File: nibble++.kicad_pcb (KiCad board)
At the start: 2 copper layers, 40 x 40 mm, 22 parts, among them SW1 SW_DPDT_x2, U1 NE555, U2 4017

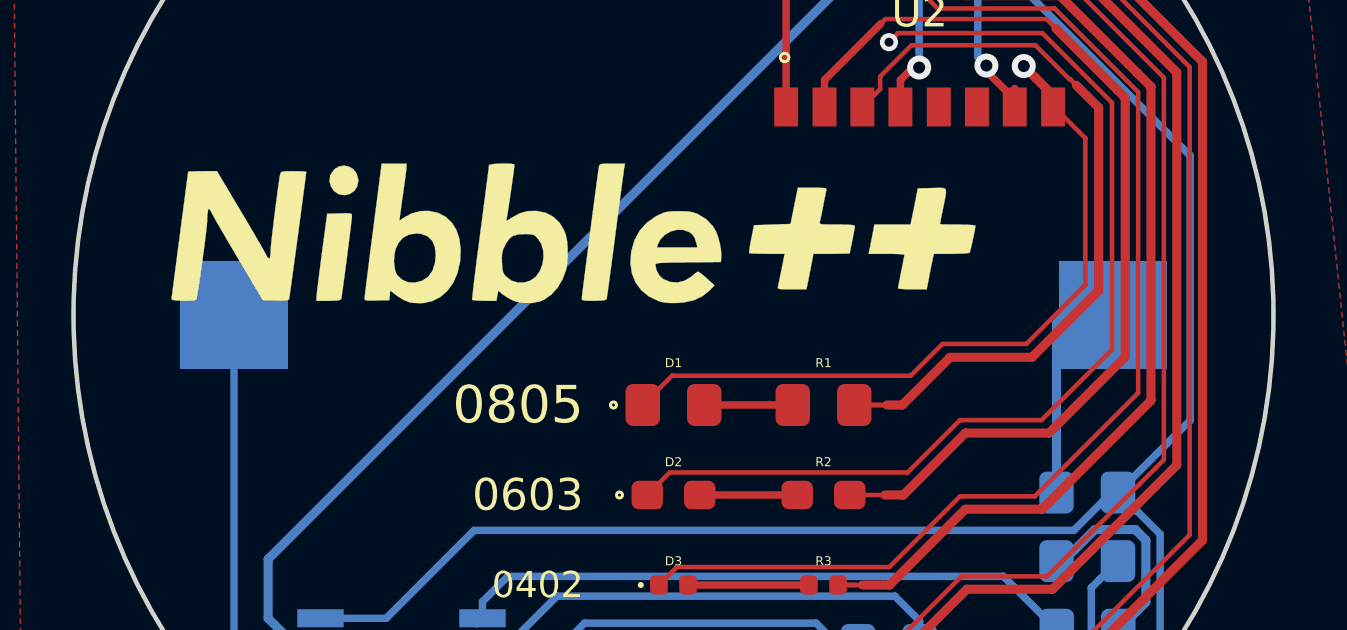
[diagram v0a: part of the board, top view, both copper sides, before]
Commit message: Renamed project to nibble++
Signed-off-by: Thomas Schmid <tom@binary-kitchen.de>
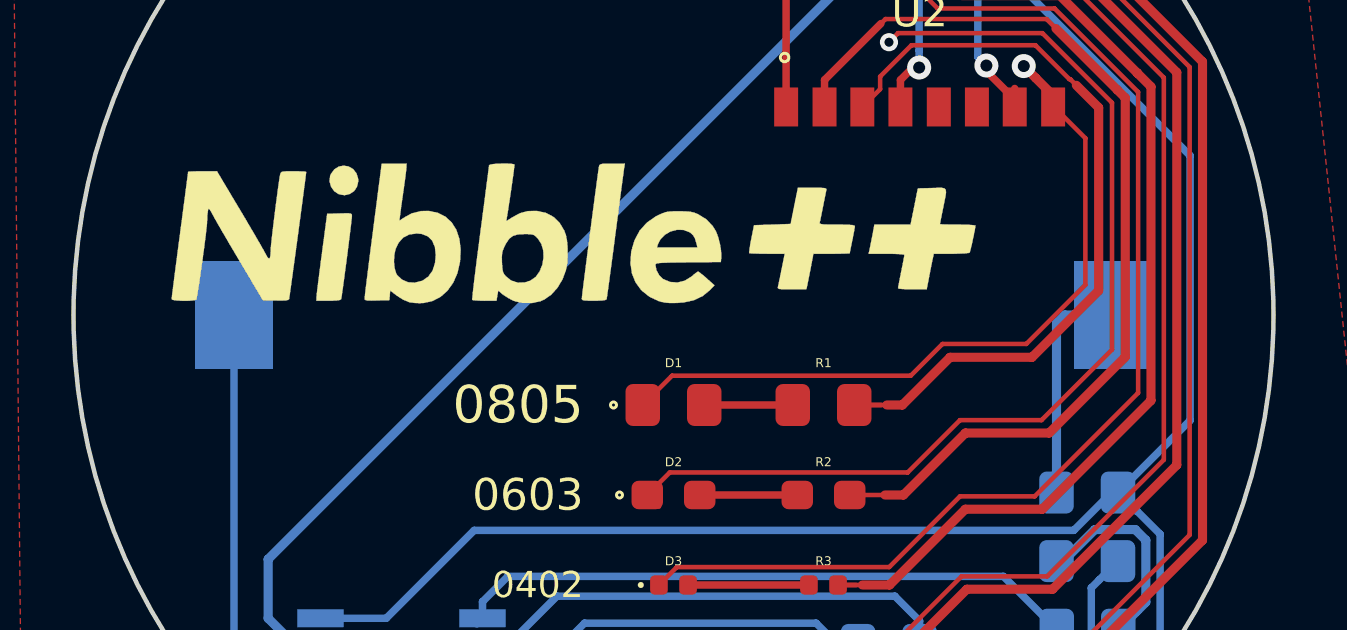
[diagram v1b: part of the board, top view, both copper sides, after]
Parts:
- BT1: footprint SMD-Challange:BatteryHolder_Keystone_1060_1x2032 -> Battery:BatteryHolder_Keystone_1060_1x2032
- D1: footprint SMD-Challange:LED_0805_2012Metric_Pad1.15x1.40mm_HandSolder_simple_drawing -> nibble++:LED_0805_2012Metric_Pad1.15x1.40mm_HandSolder_simple_drawing
- D2: footprint SMD-Challange:LED_0603_1608Metric_Pad1.05x0.95mm_HandSolder_simple_drawing -> nibble++:LED_0603_1608Metric_Pad1.05x0.95mm_HandSolder_simple_drawing
- D4, D5: footprint SMD-Challange:LED_0201_0603Metric_hand_soldering -> nibble++:LED_0201_0603Metric_hand_soldering
- R1: value R -> 100; footprint SMD-Challange:R_0805_2012Metric_Pad1.15x1.40mm_HandSolder -> nibble++:R_0805_2012Metric_Pad1.15x1.40mm_HandSolder
- R2: value R -> 100; footprint SMD-Challange:R_0603_1608Metric_Pad1.05x0.95mm_HandSolder -> nibble++:R_0603_1608Metric_Pad1.05x0.95mm_HandSolder
- R3: value R -> 100
- R4: value R -> 150; footprint SMD-Challange:R_0201_0603Metric_hand_soldering -> nibble++:R_0201_0603Metric_hand_soldering
- R5: value R -> 200; footprint SMD-Challange:R_01005_0402Metric_hand_soldering -> nibble++:R_01005_0402Metric_hand_soldering
- SW1: footprint SMD-Challange:smd_switch_slide -> nibble++:smd_switch_slide
- U2: footprint SMD-Challange:SOP-16_4.4x10.4mm_P1.27mm_simple_drawing -> nibble++:SOP-16_4.4x10.4mm_P1.27mm_simple_drawing

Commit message: fixed overlaying routes
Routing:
- net VS: track 110.8 -> 108.9 mm
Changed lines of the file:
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@@
     (thickness 1.6)
     (drawings 70)
-    (tracks 258)
+    (tracks 259)
     (zones 0)
     (modules 22)
@@
   (segment (start 103.759 86.771) (end 103.754 86.766) (width 0.25) (layer F.Cu) (net 3))
   (segment (start 103.759 88.3285) (end 103.759 86.771) (width 0.25) (layer F.Cu) (net 3))
-  (segment (start 95.881116 113.919) (end 98.927105 110.873011) (width 0.25) (layer B.Cu) (net 3))
   (segment (start 93.632 113.919) (end 95.881116 113.919) (width 0.25) (layer B.Cu) (net 3))
-  (segment (start 98.927105 110.873011) (end 103.387177 110.873011) (width 0.25) (layer B.Cu) (net 3))
-  (segment (start 103.918999 111.404833) (end 103.387177 110.873011) (width 0.25) (layer B.Cu) (net 3))
   (segment (start 104.126999 113.792) (end 103.918999 114) (width 0.25) (layer B.Cu) (net 3))
   (segment (start 106.154 113.792) (end 104.126999 113.792) (width 0.25) (layer B.Cu) (net 3))
@@
   (segment (start 103.918999 113.570999) (end 104.14 113.792) (width 0.25) (layer B.Cu) (net 3))
   (segment (start 103.918999 113.792) (end 104.14 113.792) (width 0.25) (layer B.Cu) (net 3))
-  (segment (start 103.918999 113.538) (end 103.918999 111.404833) (width 0.25) (layer B.Cu) (net 3))
   (segment (start 103.918999 113.538) (end 103.918999 113.570999) (width 0.25) (layer B.Cu) (net 3))
   (segment (start 103.918999 113.792) (end 103.918999 113.538) (width 0.25) (layer B.Cu) (net 3))
@@
   (segment (start 114.817 105.918) (end 114.6048 105.918) (width 0.25) (layer B.Cu) (net 3))
   (segment (start 114.6048 105.918) (end 113.34381 107.17899) (width 0.25) (layer B.Cu) (net 3))
+  (segment (start 97.322 111.781) (end 97.322 112.206) (width 0.25) (layer B.Cu) (net 3))
+  (segment (start 98.229989 110.873011) (end 97.322 111.781) (width 0.25) (layer B.Cu) (net 3))
+  (segment (start 103.387177 110.873011) (end 98.229989 110.873011) (width 0.25) (layer B.Cu) (net 3))
+  (segment (start 103.918999 111.404833) (end 103.387177 110.873011) (width 0.25) (layer B.Cu) (net 3))
+  (segment (start 103.918999 113.538) (end 103.918999 111.404833) (width 0.25) (layer B.Cu) (net 3))
   (segment (start 92.607 111.379) (end 93.632 111.379) (width 0.25) (layer B.Cu) (net 4))
   (segment (start 90.527 111.379) (end 92.607 111.379) (width 0.25) (layer B.Cu) (net 4))

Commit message: added additional information for some parts
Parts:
- C2: value 1µ -> 1µ F
- C3: value 100n -> 100n F
- D1: value LED -> 0805 LED Red
- D2: value LED -> 0603 LED Orange
- D3: value LED -> 0402 LED Yellow
- D4: value LED -> 0201 LED Green
- D5: value LED -> 0201 LED Blue
- R1, R2, R3: value 100 -> 100 Ohm
- R4: value 150 -> 150 Ohm
- R5: value 200 -> 200 Ohm
- R6, R7: value 100k -> 100k Ohm
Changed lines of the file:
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@@
       (effects (font (size 0.3 0.3) (thickness 0.075)))
     )
-    (fp_text value 100 (at 0 1.43) (layer F.Fab)
+    (fp_text value "100 Ohm" (at 0 1.43) (layer F.Fab)
       (effects (font (size 1 1) (thickness 0.15)))
     )
@@
       (effects (font (size 0.3 0.3) (thickness 0.075)))
     )
-    (fp_text value 100 (at 0 1.65) (layer F.Fab)
+    (fp_text value "100 Ohm" (at 0 1.65) (layer F.Fab)
       (effects (font (size 1 1) (thickness 0.15)))
     )
@@
       (effects (font (size 1 1) (thickness 0.15)) (justify mirror))
     )
-    (fp_text value 1µ (at 0 -1.65) (layer B.Fab)
+    (fp_text value "1µ F" (at 0 -1.65) (layer B.Fab)
       (effects (font (size 1 1) (thickness 0.15)) (justify mirror))
     )
@@
       (effects (font (size 1 1) (thickness 0.15)) (justify mirror))
     )
-    (fp_text value 100n (at 0 -1.65) (layer B.Fab)
+    (fp_text value "100n F" (at 0 -1.65) (layer B.Fab)
       (effects (font (size 1 1) (thickness 0.15)) (justify mirror))
     )
@@
       (effects (font (size 0.3 0.3) (thickness 0.075)))
     )
-    (fp_text value LED (at 0 1.17) (layer F.Fab)
+    (fp_text value "0402 LED Yellow" (at 0 1.17) (layer F.Fab)
       (effects (font (size 1 1) (thickness 0.15)))
     )
@@
       (effects (font (size 1 1) (thickness 0.15)) (justify mirror))
     )
-    (fp_text value 100k (at 0 -1.65) (layer B.Fab)
+    (fp_text value "100k Ohm" (at 0 -1.65) (layer B.Fab)
       (effects (font (size 1 1) (thickness 0.15)) (justify mirror))
     )
@@
       (effects (font (size 1 1) (thickness 0.15)) (justify mirror))
     )
-    (fp_text value 100k (at 0 -1.65) (layer B.Fab)
+    (fp_text value "100k Ohm" (at 0 -1.65) (layer B.Fab)
       (effects (font (size 1 1) (thickness 0.15)) (justify mirror))
     )
@@
       (effects (font (size 0.3 0.3) (thickness 0.075)))
     )
-    (fp_text value 100 (at 0 1.17) (layer F.Fab)
+    (fp_text value "100 Ohm" (at 0 1.17) (layer F.Fab)
       (effects (font (size 1 1) (thickness 0.15)))
     )
@@
       (effects (font (size 0.3 0.3) (thickness 0.075)))
     )
-    (fp_text value LED (at 0 1.65) (layer F.Fab)
+    (fp_text value "0805 LED Red" (at 0 1.65) (layer F.Fab)
       (effects (font (size 1 1) (thickness 0.15)))
     )
@@
       (effects (font (size 0.3 0.3) (thickness 0.075)))
     )
-    (fp_text value LED (at 0 1.43) (layer F.Fab)
+    (fp_text value "0603 LED Orange" (at 0 1.43) (layer F.Fab)
       (effects (font (size 1 1) (thickness 0.15)))
     )
@@
       (effects (font (size 0.3 0.3) (thickness 0.075)))
     )
-    (fp_text value LED (at 0 1.05) (layer F.Fab)
+    (fp_text value "0201 LED Green" (at 0 1.05) (layer F.Fab)
       (effects (font (size 1 1) (thickness 0.15)))
     )
@@
       (effects (font (size 0.3 0.3) (thickness 0.075)))
     )
-    (fp_text value LED (at 0 1.05) (layer F.Fab)
+    (fp_text value "0201 LED Blue" (at 0 1.05) (layer F.Fab)
       (effects (font (size 1 1) (thickness 0.15)))
     )
@@
       (effects (font (size 0.3 0.3) (thickness 0.075)))
     )
-    (fp_text value 150 (at 0 1.05) (layer F.Fab)
+    (fp_text value "150 Ohm" (at 0 1.05) (layer F.Fab)
       (effects (font (size 1 1) (thickness 0.15)))
     )
@@
       (effects (font (size 0.3 0.3) (thickness 0.075)))
     )
-    (fp_text value 200 (at 0 1) (layer F.Fab)
-      (effects (font (size 1 1) (thickness 0.15)))
-    )
+    (fp_text value "200 Ohm" (at 0 1) (layer F.Fab)
+      (effects (font (size 1 1) (thickness 0.15)))
+    )
